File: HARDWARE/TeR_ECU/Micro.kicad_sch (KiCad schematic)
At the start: 23 parts, among them J1 Debug, SW1 RST, U1 STM32F446RETx, Y1 Crystal

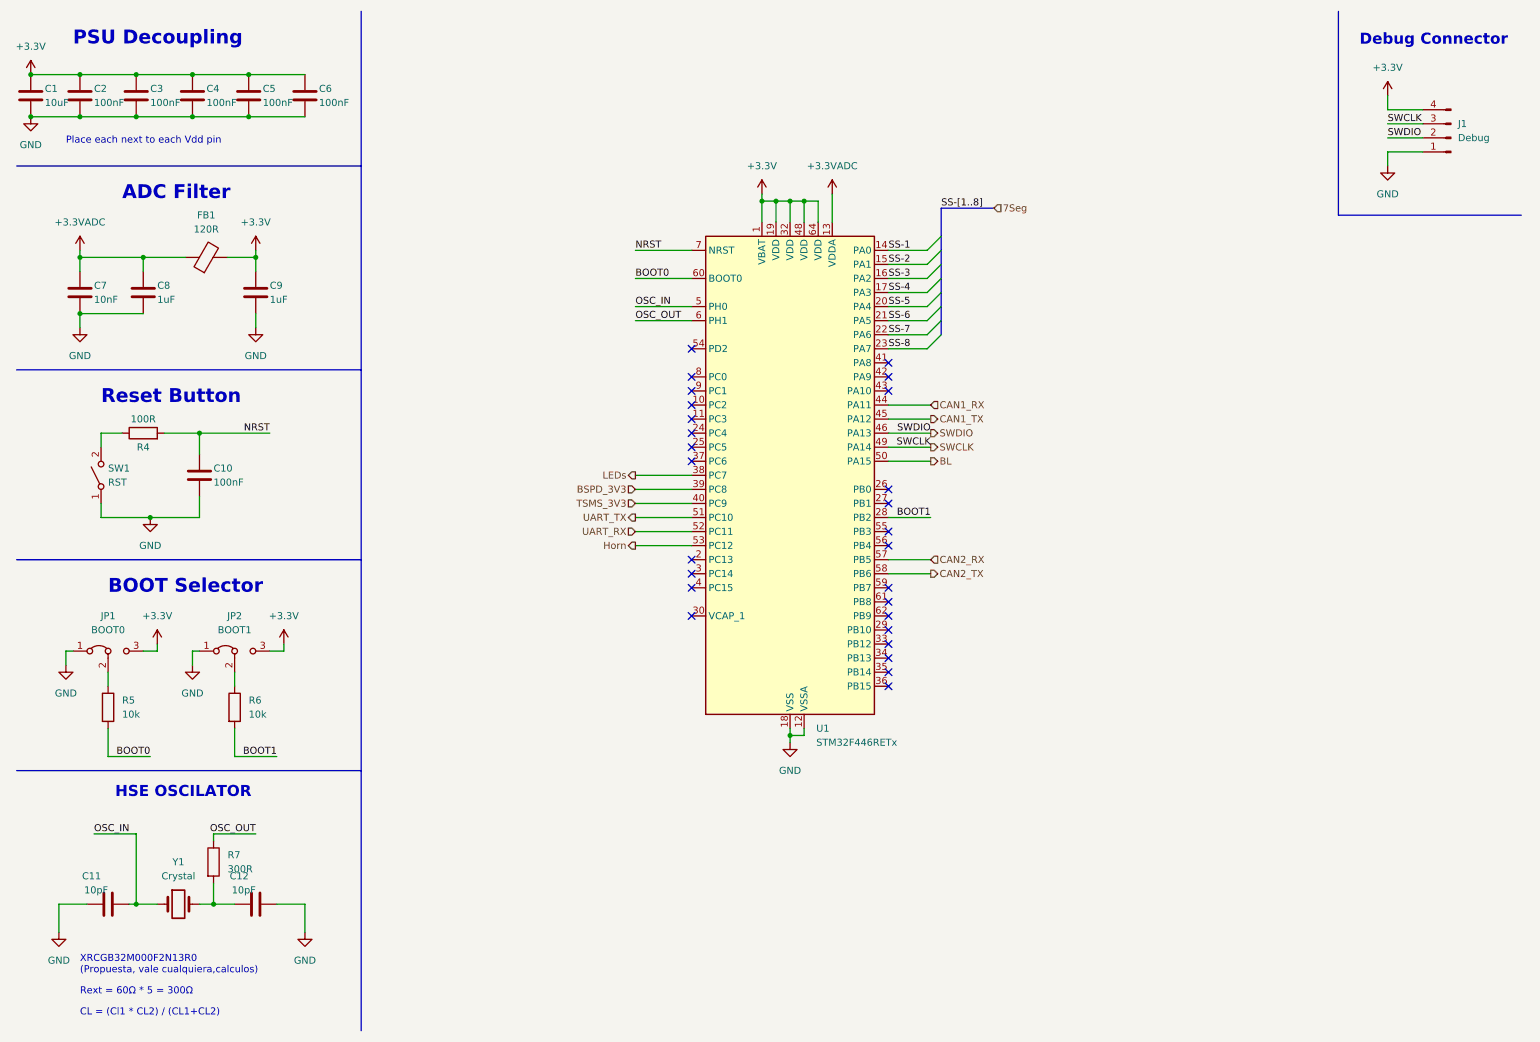
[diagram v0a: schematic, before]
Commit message: Layout V2, added 7-segment display, optimal placement of pins + rework of the boot headers(just one needed)
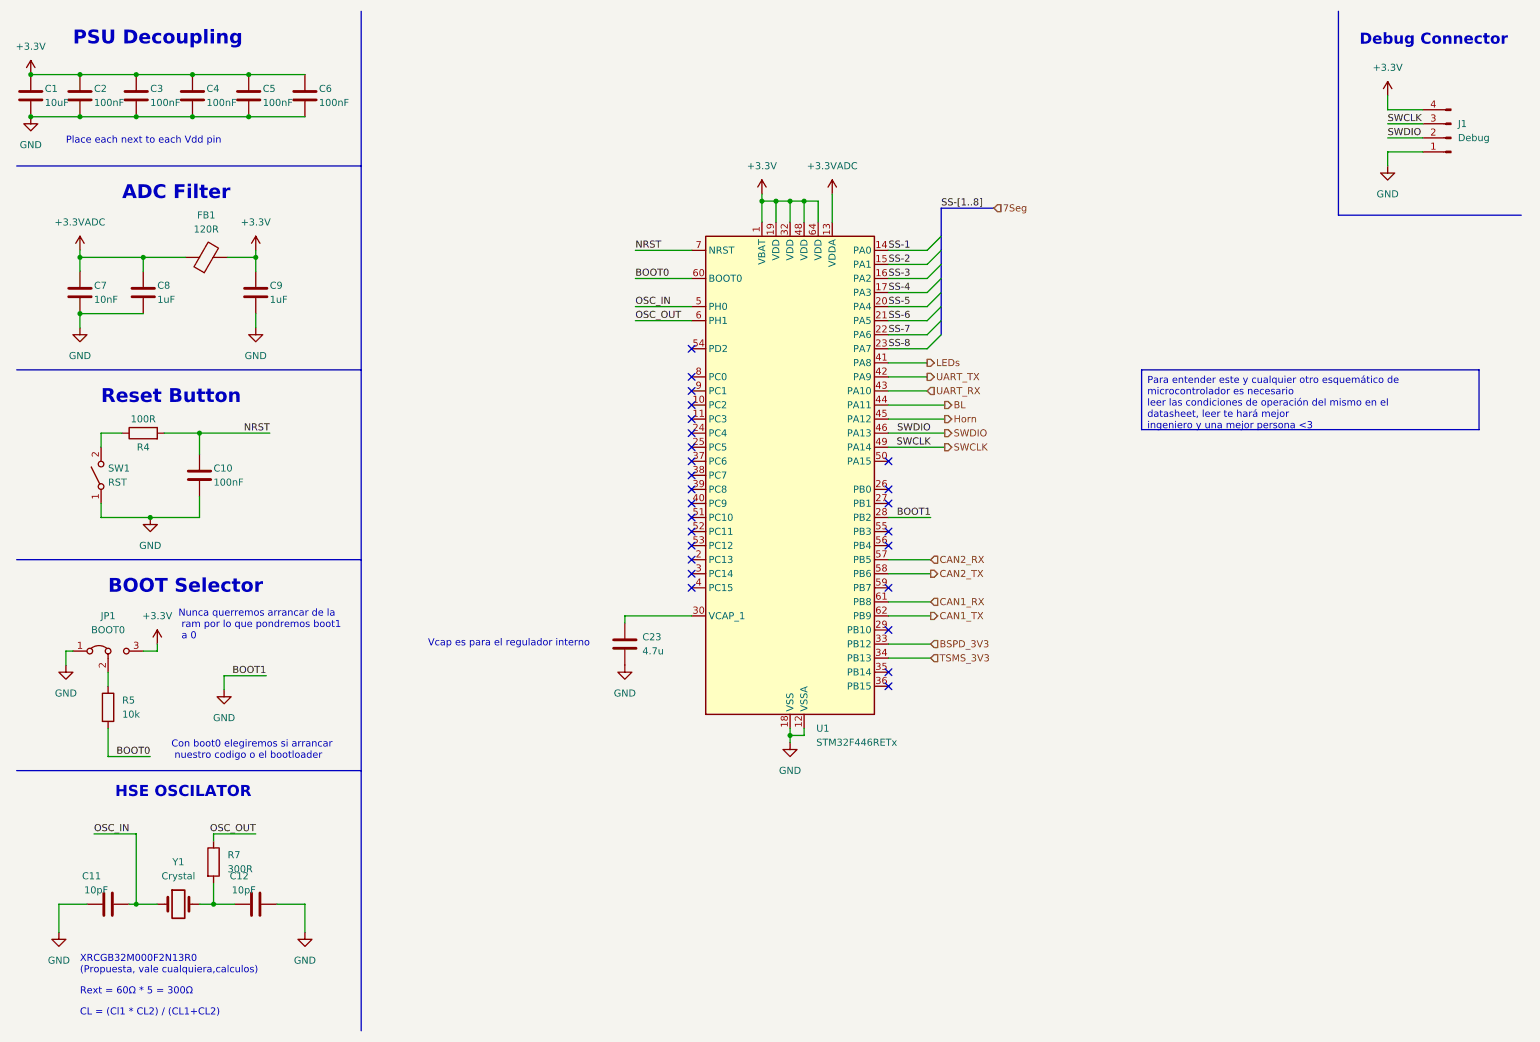
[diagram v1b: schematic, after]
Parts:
- removed JP2: BOOT1, Connector_PinHeader_2.00mm:PinHeader_1x03_P2.00mm_Vertical, symbol Jumper:Jumper_3_Bridged12
- removed R6: 10k, Resistor_SMD:R_0603_1608Metric, symbol Device:R
- added C23: 4.7u, Capacitor_SMD:C_0805_2012Metric, symbol Device:C
- C7: footprint Capacitor_SMD:C_0603_1608Metric -> Capacitor_SMD:C_0402_1005Metric
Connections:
- net BOOT1 is gone; now on net GND: U1.28 (PB2)
- net BL: now also U1.44 (PA11); no longer U1.50 (PA15)
- net BSPD_3V3: now also U1.33 (PB12); no longer U1.39 (PC8)
- net CAN1_RX: now also U1.61 (PB8); no longer U1.44 (PA11)
- net CAN1_TX: now also U1.62 (PB9); no longer U1.45 (PA12)
- net GND: now also C23.2
- net Horn: now also U1.45 (PA12); no longer U1.53 (PC12)
- net LEDs: now also U1.41 (PA8); no longer U1.38 (PC7)
- net TSMS_3V3: now also U1.34 (PB13); no longer U1.40 (PC9)
- net UART_RX: now also U1.43 (PA10); no longer U1.52 (PC11)
- net UART_TX: now also U1.42 (PA9); no longer U1.51 (PC10)
- net at U1.30 (VCAP_1): now also C23.1
- no-connect marks 27 -> 26
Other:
- note added: "Con boot0 elegiremos si arrancar nuestro codigo o el bootloader"
- note added: "Nunca querremos arrancar de la ram por lo que pondremos boot1 a 0"
- note added: "Vcap es para el regulador interno"

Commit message: Rethought project using an STM32NucleoF7
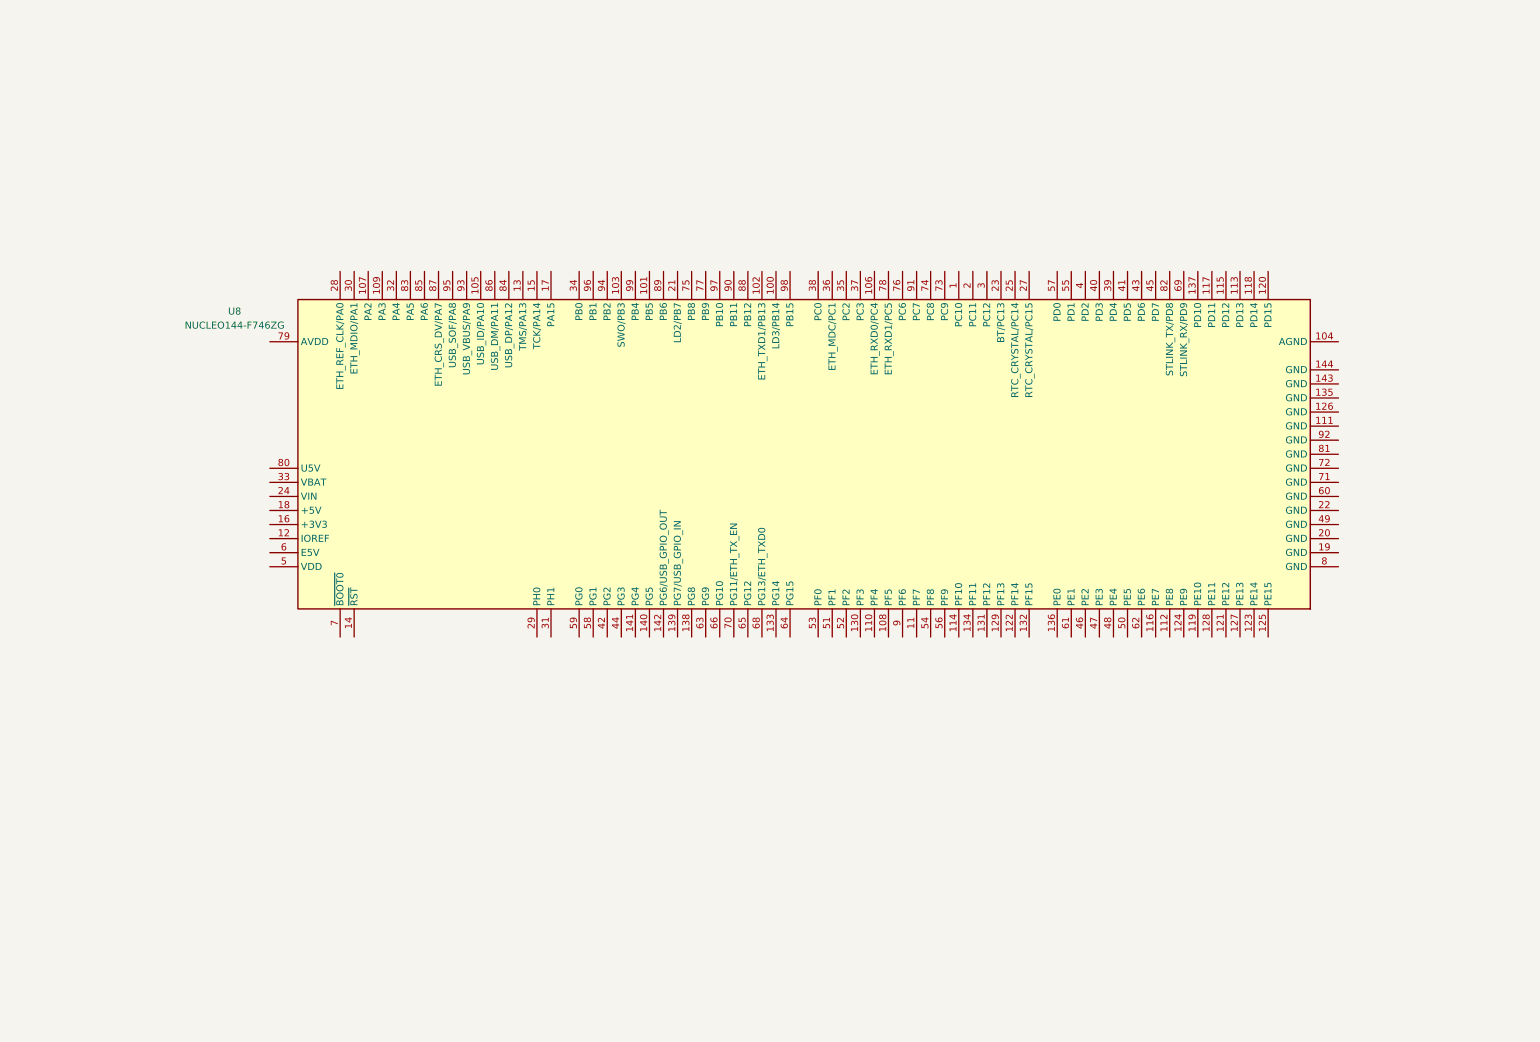
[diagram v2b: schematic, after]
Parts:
- removed C1: 10uF, Capacitor_SMD:C_0805_2012Metric, symbol Device:C
- removed C10: 100nF, Capacitor_SMD:C_0603_1608Metric, symbol Device:C
- removed C11, C12: 10pF, Capacitor_SMD:C_0603_1608Metric, symbol Device:C
- removed C2, C3, C4, C5, C6: 100nF, Capacitor_SMD:C_0402_1005Metric, symbol Device:C
- removed C23: 4.7u, Capacitor_SMD:C_0805_2012Metric, symbol Device:C
- removed C7: 10nF, Capacitor_SMD:C_0402_1005Metric, symbol Device:C
- removed C8, C9: 1uF, Capacitor_SMD:C_0603_1608Metric, symbol Device:C
- removed FB1: 120R, Inductor_SMD:L_0805_2012Metric, symbol Device:FerriteBead
- removed J1: Debug, Connector_PinHeader_2.00mm:PinHeader_1x04_P2.00mm_Vertical, symbol Connector:Conn_01x04_Pin
- removed JP1: BOOT0, Connector_PinHeader_2.00mm:PinHeader_1x03_P2.00mm_Vertical, symbol Jumper:Jumper_3_Bridged12
- removed R4: 100R, Resistor_SMD:R_0603_1608Metric, symbol Device:R
- removed R5: 10k, Resistor_SMD:R_0603_1608Metric, symbol Device:R
- removed R7: 300R, Resistor_SMD:R_0402_1005Metric, symbol Device:R
- removed SW1: RST, Button_Switch_SMD:SW_Tactile_SPST_NO_Straight_CK_PTS636Sx25SMTRLFS, symbol Switch:SW_SPST
- removed U1: STM32F446RETx, Package_QFP:LQFP-64_10x10mm_P0.5mm, symbol MCU_ST_STM32F4:STM32F446RETx
- removed Y1: Crystal, Crystal:Crystal_SMD_5032-2Pin_5.0x3.2mm, symbol Device:Crystal
- added U8: NUCLEO144-F746ZG, Module:ST_Morpho_Connector_144_STLink, symbol MCU_Module:NUCLEO144-F746ZG
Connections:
- no-connect marks 26 -> 0
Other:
- note removed: "ADC Filter"
- note removed: "BOOT Selector"
- note removed: "CL = (Cl1 * CL2) / (CL1+CL2)"
- note removed: "Con boot0 elegiremos si arrancar nuestro codigo o el bootloader"
- note removed: "Debug Connector"
- note removed: "HSE OSCILATOR"
- note removed: "Nunca querremos arrancar de la ram por lo que pondremos boot1 a 0"
- note removed: "PSU Decoupling"
- note removed: "Place each next to each Vdd pin"
- note removed: "Reset Button"
- note removed: "Rext = 60Ω * 5 = 300Ω"
- note removed: "Vcap es para el regulador interno"
- note removed: "XRCGB32M000F2N13R0 (Propuesta, vale cualquiera,calculos)"

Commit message: Cambiando micro
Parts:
- removed U8: NUCLEO144-F746ZG, Module:ST_Morpho_Connector_144_STLink, symbol MCU_Module:NUCLEO144-F746ZG
- added U1: NUCLEO-F446RE, Nucleo-F446RE:MODULE_NUCLEO-F446RE, symbol NUCLEO-F446RE:NUCLEO-F446RE
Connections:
- new net +5V: U1.CN7_6 (E5V)
- new net GND: U1.CN7_19 (CN7_GND), U1.CN7_20 (CN7_GND), U1.CN7_22 (CN7_GND), U1.CN7_8 (CN7_GND)

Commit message: Empezando Layout
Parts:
- added unit 4 of U1
- added unit 3 of U1
- added unit 5 of U1
- added unit 6 of U1
- added unit 2 of U1
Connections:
- net GND: now also U1.CN10_20 (CN10_GND), U1.CN10_32 (AGND), U1.CN10_9 (CN10_GND)
- net UART_TX: now reaches U1.CN7_1 (PC10)
- net UART_RX: now reaches U1.CN7_2 (PC11)
- net BL: now reaches U1.CN7_21 (PB7)
- net Horn: now reaches U1.CN7_34 (PB0)
- new net: U1.CN6_6 (CN6_GND), U1.CN6_7 (CN6_GND)
- new net BSPD_3V3: U1.CN10_31 (PB3)
- new net CAN1_RX: U1.CN10_3 (PB8)
- new net CAN1_TX: U1.CN10_5 (PB9)
- new net CAN2_RX: U1.CN10_29 (PB5)
- new net CAN2_TX: U1.CN10_17 (PB6)
- new net TSMS_3V3: U1.CN10_27 (PB4)
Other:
- note added: "CAN1 El del PowerTrain CAN2 El Main del coche"
- moved on the sheet: U1A

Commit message: Layout acabado
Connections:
- net BSPD_3V3: now also U1.CN7_34 (PB0); no longer U1.CN10_31 (PB3)
- net Horn: now also U1.CN7_30 (PA1); no longer U1.CN7_34 (PB0)
- net TSMS_3V3: now also U1.CN7_32 (PA4); no longer U1.CN10_27 (PB4)
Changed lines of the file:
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@@
-    (stroke (width 0) (type default))
-  )
-  (wire (pts (xy 130.81 99.06) (xy 133.35 99.06))
     (stroke (width 0) (type default))
   )
@@
     (stroke (width 0) (type default))
   )
+  (wire (pts (xy 31.75 87.63) (xy 34.29 87.63))
+    (stroke (width 0) (type default))
+  )
+  (wire (pts (xy 31.75 85.09) (xy 34.29 85.09))
+    (stroke (width 0) (type default))
+  )
   (wire (pts (xy 168.91 130.81) (xy 176.53 130.81))
     (stroke (width 0) (type default))
@@
     (stroke (width 0) (type default))
   )
-  (wire (pts (xy 31.75 100.33) (xy 34.29 100.33))
-    (stroke (width 0) (type default))
-  )
   (wire (pts (xy 80.01 135.89) (xy 83.82 135.89))
     (stroke (width 0) (type default))
   )
-  (wire (pts (xy 130.81 101.6) (xy 133.35 101.6))
+  (wire (pts (xy 31.75 100.33) (xy 34.29 100.33))
     (stroke (width 0) (type default))
   )
@@
     (effects (font (size 1.27 1.27)) (justify right))
   )
-  (hierarchical_label "BSPD_3V3" (shape input) (at 130.81 99.06 180) (fields_autoplaced)
+  (hierarchical_label "BSPD_3V3" (shape input) (at 31.75 100.33 180) (fields_autoplaced)
     (effects (font (size 1.27 1.27)) (justify right))
   )
@@
     (effects (font (size 1.27 1.27)) (justify right))
   )
-  (hierarchical_label "TSMS_3V3" (shape input) (at 130.81 101.6 180) (fields_autoplaced)
+  (hierarchical_label "TSMS_3V3" (shape input) (at 31.75 87.63 180) (fields_autoplaced)
     (effects (font (size 1.27 1.27)) (justify right))
   )
-  (hierarchical_label "Horn" (shape output) (at 31.75 100.33 180) (fields_autoplaced)
+  (hierarchical_label "Horn" (shape output) (at 31.75 85.09 180) (fields_autoplaced)
     (effects (font (size 1.27 1.27)) (justify right))
   )

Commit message: Layout acabado
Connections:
- net BL: now also U1.CN7_30 (PA1); no longer U1.CN7_21 (PB7)
- net Horn: now also U1.CN7_21 (PB7); no longer U1.CN7_30 (PA1)
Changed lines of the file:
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@@
   (junction (at 168.91 130.81) (diameter 0) (color 0 0 0 0)
+  )
+  (wire (pts (xy 31.75 102.87) (xy 34.29 102.87))
+    (stroke (width 0) (type default))
+  )
+  (wire (pts (xy 31.75 85.09) (xy 34.29 85.09))
+    (stroke (width 0) (type default))
   )
   (wire (pts (xy 80.01 62.23) (xy 85.09 62.23))
@@
     (stroke (width 0) (type default))
   )
-  (wire (pts (xy 176.53 130.81) (xy 176.53 132.08))
+  (wire (pts (xy 31.75 87.63) (xy 34.29 87.63))
     (stroke (width 0) (type default))
   )
-  (wire (pts (xy 31.75 102.87) (xy 34.29 102.87))
+  (wire (pts (xy 176.53 130.81) (xy 176.53 132.08))
     (stroke (width 0) (type default))
   )
@@
   )
   (wire (pts (xy 168.91 129.54) (xy 168.91 130.81))
-    (stroke (width 0) (type default))
-  )
-  (wire (pts (xy 31.75 87.63) (xy 34.29 87.63))
-    (stroke (width 0) (type default))
-  )
-  (wire (pts (xy 31.75 85.09) (xy 34.29 85.09))
     (stroke (width 0) (type default))
   )
@@
     (effects (font (size 1.27 1.27)) (justify right))
   )
-  (hierarchical_label "BL" (shape output) (at 31.75 102.87 180) (fields_autoplaced)
+  (hierarchical_label "BL" (shape output) (at 31.75 85.09 180) (fields_autoplaced)
     (effects (font (size 1.27 1.27)) (justify right))
   )
@@
     (effects (font (size 1.27 1.27)) (justify right))
   )
-  (hierarchical_label "Horn" (shape output) (at 31.75 85.09 180) (fields_autoplaced)
+  (hierarchical_label "Horn" (shape output) (at 31.75 102.87 180) (fields_autoplaced)
     (effects (font (size 1.27 1.27)) (justify right))
   )
